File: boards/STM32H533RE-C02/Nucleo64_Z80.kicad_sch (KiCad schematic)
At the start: 12 parts, among them U2 AS6C4008-55PCN, U3 Z80CPU

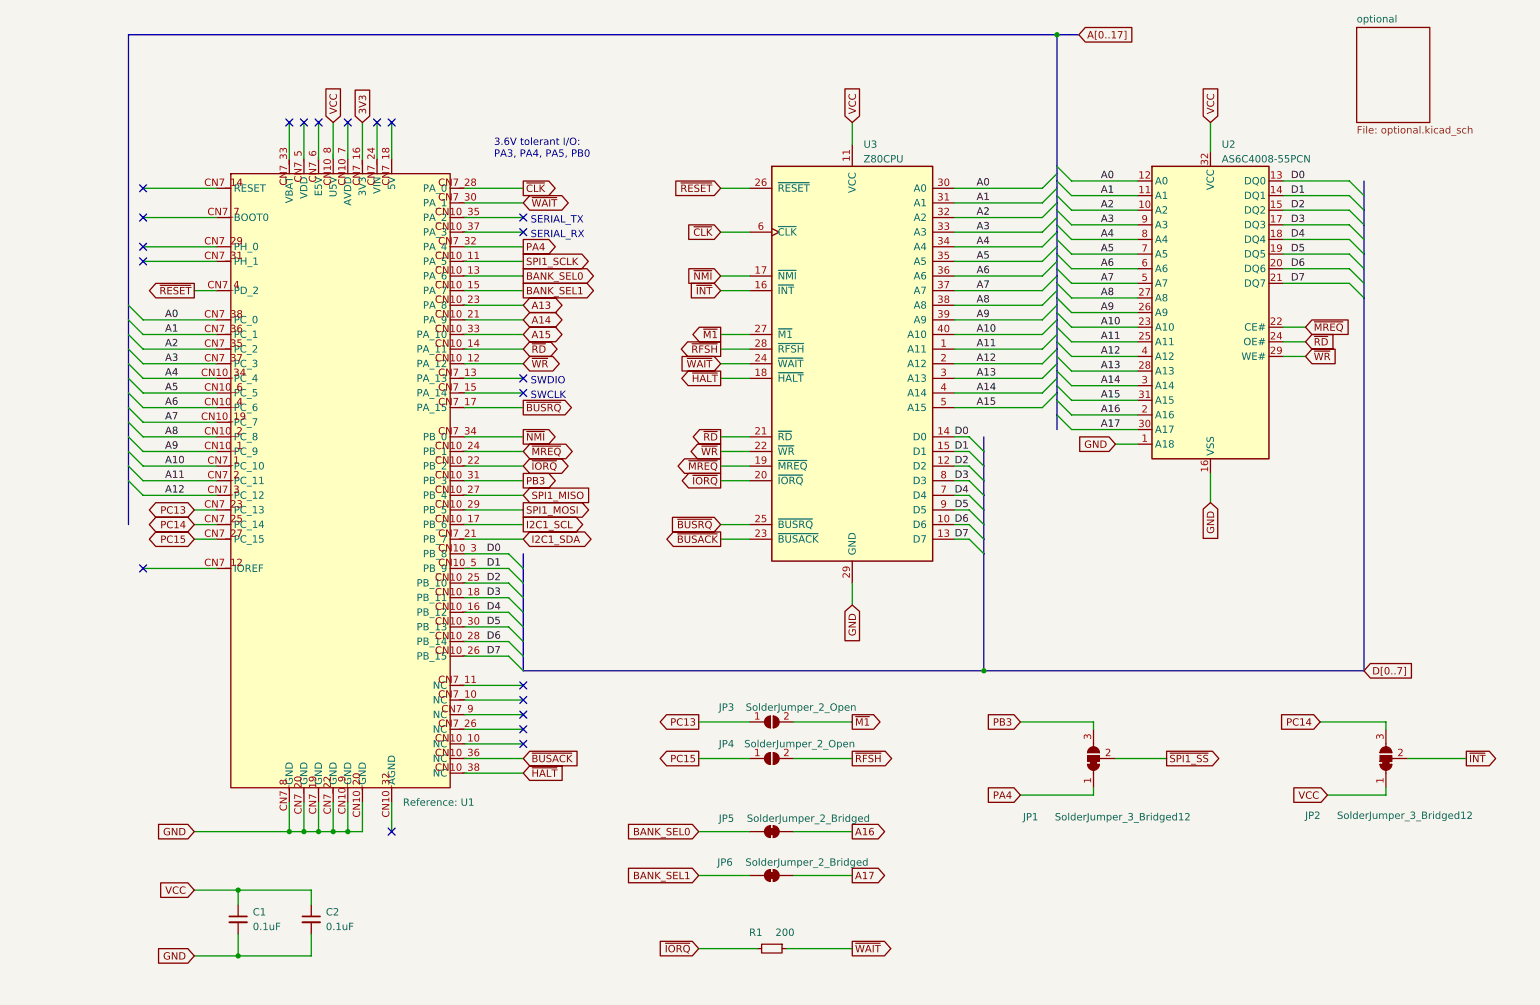
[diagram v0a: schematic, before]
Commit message: stm32h533re: Fix schematics
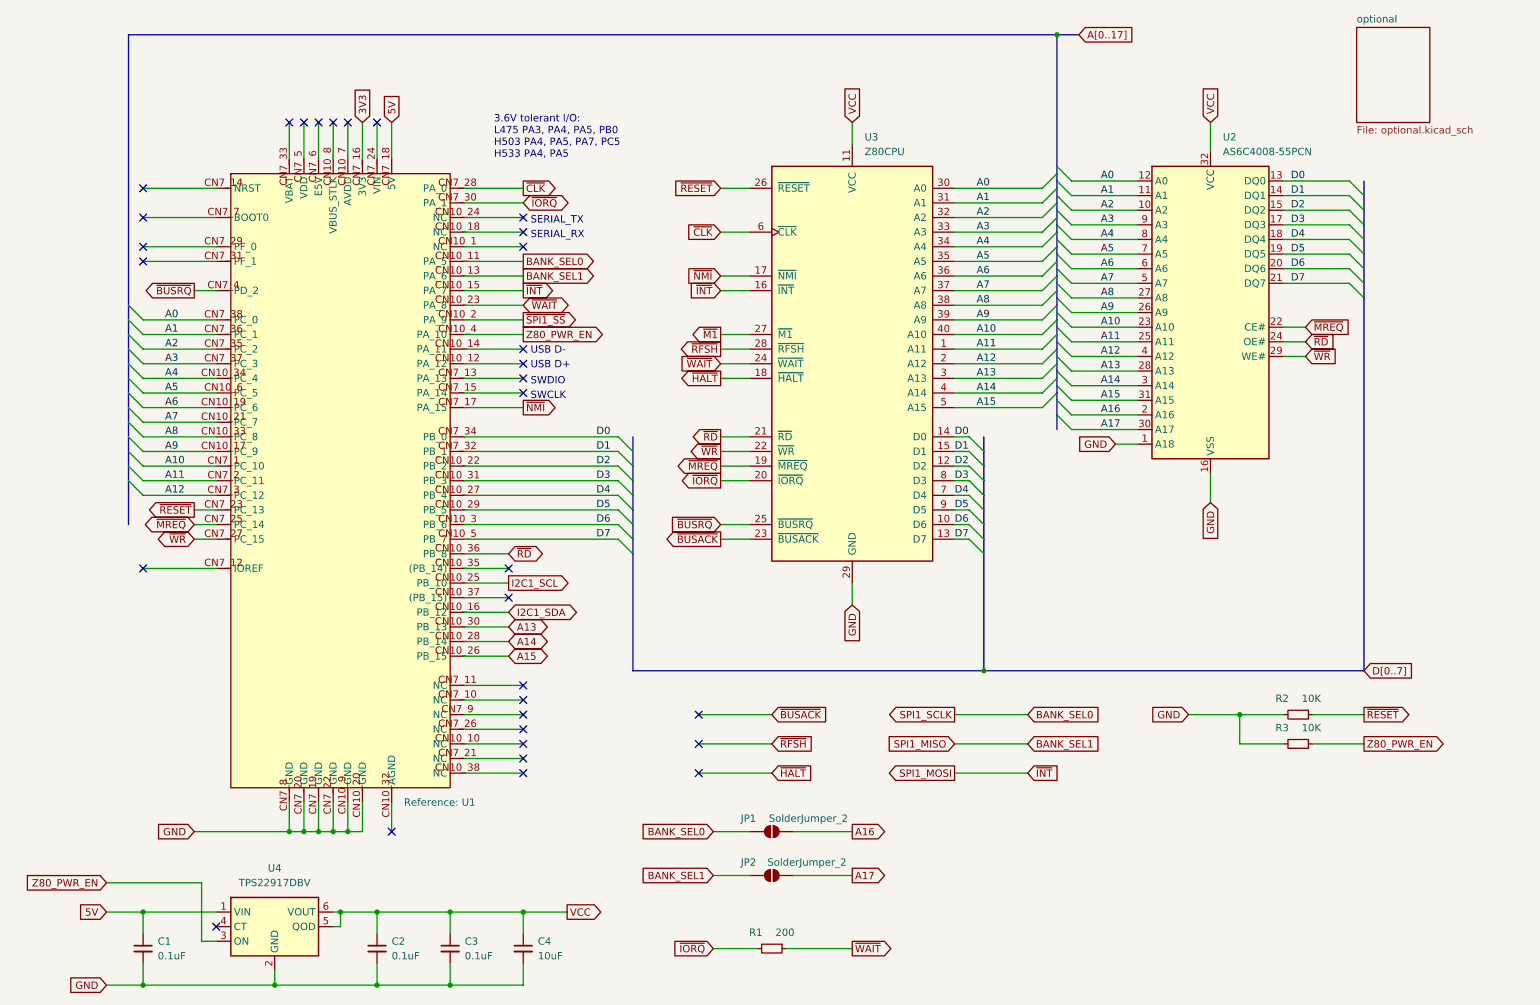
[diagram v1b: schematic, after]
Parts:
- removed JP1, JP2: SolderJumper_3_Bridged12, Jumper:SolderJumper-3_P1.3mm_Bridged12_RoundedPad1.0x1.5mm_NumberLabels, symbol Jumper:SolderJumper_3_Bridged12
- removed JP3, JP4: SolderJumper_2_Open, Jumper:SolderJumper-2_P1.3mm_Open_RoundedPad1.0x1.5mm, symbol Jumper:SolderJumper_2_Open
- added C1: 0.1uF, Capacitor_THT:C_Disc_D3.8mm_W2.6mm_P2.50mm, symbol Device:C_Small
- added C4: 10uF, Capacitor_THT:CP_Radial_D5.0mm_P2.50mm, symbol Device:C_Small
- added R2, R3: 10K, Resistor_SMD:R_0603_1608Metric_Pad0.98x0.95mm_HandSolder, symbol Device:R_Small
- added U4: TPS22917DBV, Package_TO_SOT_SMD:SOT-23-6, symbol Power_Management:TPS22917DBV
- JP1: renamed from JP5; value SolderJumper_2_Bridged -> SolderJumper_2; footprint Jumper:SolderJumper-2_P1.3mm_Bridged_RoundedPad1.0x1.5mm -> Jumper:SolderJumper-2_P1.3mm_Open_TrianglePad1.0x1.5mm; symbol Jumper:SolderJumper_2_Bridged -> Jumper:SolderJumper_2_Open
- JP2: renamed from JP6; value SolderJumper_2_Bridged -> SolderJumper_2; footprint Jumper:SolderJumper-2_P1.3mm_Bridged_RoundedPad1.0x1.5mm -> Jumper:SolderJumper-2_P1.3mm_Open_TrianglePad1.0x1.5mm; symbol Jumper:SolderJumper_2_Bridged -> Jumper:SolderJumper_2_Open
- U1: symbol mylib:NUCLEO-L476RG -> library:NUCLEO-H533RE
- U2: symbol Memory_RAM:AS6C4008-55PCN -> library:AS6C4008-55PCN
- U3: symbol CPU:Z80CPU -> library:Z80CPU
- renumbered C1 to C2, C2 to C3
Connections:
- net PA4 is gone; now on net D1: U1.CN7_32 (PB_1)
- net PB3 is gone; now on net D3: U1.CN10_31 (PB_3)
- net PC13 is gone; now on net ~{RESET}: U1.CN7_23 (PC_13)
- net PC14 is gone; now on net ~{MREQ}: U1.CN7_25 (PC_14)
- net PC15 is gone; now on net ~{WR}: U1.CN7_27 (PC_15)
- net SPI1_MISO is gone; now on net D4: U1.CN10_27 (PB_4)
- net SPI1_SCLK is gone; now on net BANK_SEL0: U1.CN10_11 (PA_5)
- net ~{INT} is gone; now on net SPI1_MOSI: U3.16 (~{INT})
- net A13: now also U1.CN10_30 (PB_13); no longer U1.CN10_23 (PA_8)
- net A14: now also U1.CN10_28 (PB_14); no longer U1.CN10_21 (PA_9)
- net A15: now also U1.CN10_26 (PB_15); no longer U1.CN10_33 (PA_10)
- net A6: now also U1.CN10_19 (PC_6); no longer U1.CN10_4 (PC_6)
- net A7: now also U1.CN10_21 (PC_7); no longer U1.CN10_19 (PC_7)
- net A8: now also U1.CN10_33 (PC_8); no longer U1.CN10_2 (PC_8)
- net A9: now also U1.CN10_17 (PC_9); no longer U1.CN10_1 (PC_9)
- net BANK_SEL0: no longer U1.CN10_13 (PA_6)
- net BANK_SEL1: now also U1.CN10_13 (PA_6); no longer U1.CN10_15 (PA_7)
- net D0: now also U1.CN7_34 (PB_0); no longer U1.CN10_3 (PB_8)
- net D1: no longer U1.CN10_5 (PB_9)
- net D2: now also U1.CN10_22 (PB_2); no longer U1.CN10_25 (PB_10)
- net D3: no longer U1.CN10_18 (PB_11)
- net D4: no longer U1.CN10_16 (PB_12)
- net D5: now also U1.CN10_29 (PB_5); no longer U1.CN10_30 (PB_13)
- net D6: now also U1.CN10_3 (PB_6); no longer U1.CN10_28 (PB_14)
- net D7: now also U1.CN10_5 (PB_7); no longer U1.CN10_26 (PB_15)
- net GND: now also C1.2, C4.2, R2.2, R3.2, U4.2 (GND)
- net I2C1_SCL: now also U1.CN10_25 (PB_10); no longer U1.CN10_17 (PB_6)
- net I2C1_SDA: now also U1.CN10_16 (PB_12); no longer U1.CN7_21 (PB_7)
- net SPI1_MOSI: now also U1.CN10_15 (PA_7); no longer U1.CN10_29 (PB_5)
- net VCC: now also C4.1, U4.5 (QOD), U4.6 (VOUT); no longer U1.CN10_8 (U5V)
- net ~{BUSACK}: no longer U1.CN10_36 (NC)
- net ~{BUSRQ}: now also U1.CN7_4 (PD_2); no longer U1.CN7_17 (PA_15)
- net ~{HALT}: no longer U1.CN10_38 (NC)
- net ~{IORQ}: now also U1.CN7_30 (PA_1); no longer U1.CN10_22 (PB_2)
- net ~{MREQ}: no longer U1.CN10_24 (PB_1)
- net ~{NMI}: now also U1.CN7_17 (PA_15); no longer U1.CN7_34 (PB_0)
- net ~{RD}: now also U1.CN10_36 (PB_8); no longer U1.CN10_14 (PA_11)
- net ~{RESET}: now also R2.1; no longer U1.CN7_4 (PD_2)
- net ~{SPI1_SS}: now also U1.CN10_2 (PA_9)
- net ~{WAIT}: now also U1.CN10_23 (PA_8); no longer U1.CN7_30 (PA_1)
- net ~{WR}: no longer U1.CN10_12 (PA_12)
- net 5V: now reaches U1.CN7_18 (5V)
- net 5V: now also C1.1, U4.1 (VIN)
- new net Z80_PWR_EN: R3.1, U1.CN10_4 (PA_10), U4.3 (ON)
- no-connect marks 21 -> 32
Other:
- note added: "3.6V tolerant I/O: L475 PA3, PA4, PA5, PB0 H503 PA4, PA5, PA7, PC5 H533 PA4, PA5"
- note added: "USB D+"
- note added: "USB D-"
- note removed: "3.6V tolerant I/O: PA3, PA4, PA5, PB0"
- title: Nucleo64 Z80 -> Nucleo64 Z80 (H533)
- moved on the sheet: C2, C3

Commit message: stm32h533re: Fix PCB layout
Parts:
- C1: footprint Capacitor_THT:C_Disc_D3.8mm_W2.6mm_P2.50mm -> Capacitor_SMD:C_0603_1608Metric_Pad1.08x0.95mm_HandSolder
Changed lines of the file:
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@@
 			)
 		)
-		(property "Footprint" "Capacitor_THT:C_Disc_D3.8mm_W2.6mm_P2.50mm"
+		(property "Footprint" "Capacitor_SMD:C_0603_1608Metric_Pad1.08x0.95mm_HandSolder"
 			(at 39.37 182.88 0)
 			(effects
